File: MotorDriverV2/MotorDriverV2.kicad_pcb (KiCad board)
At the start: 2 copper layers, 20 parts, among them IC1 DRV8871DDARQ1, IC2 DRV8871DDARQ1, IC3 ESP32-S3-WROOM-1U-N4, J1 Power, J2 Out_A, J3 Conn_01x10_Pin, J4 Out_B, U1 USBLC6-2SC6

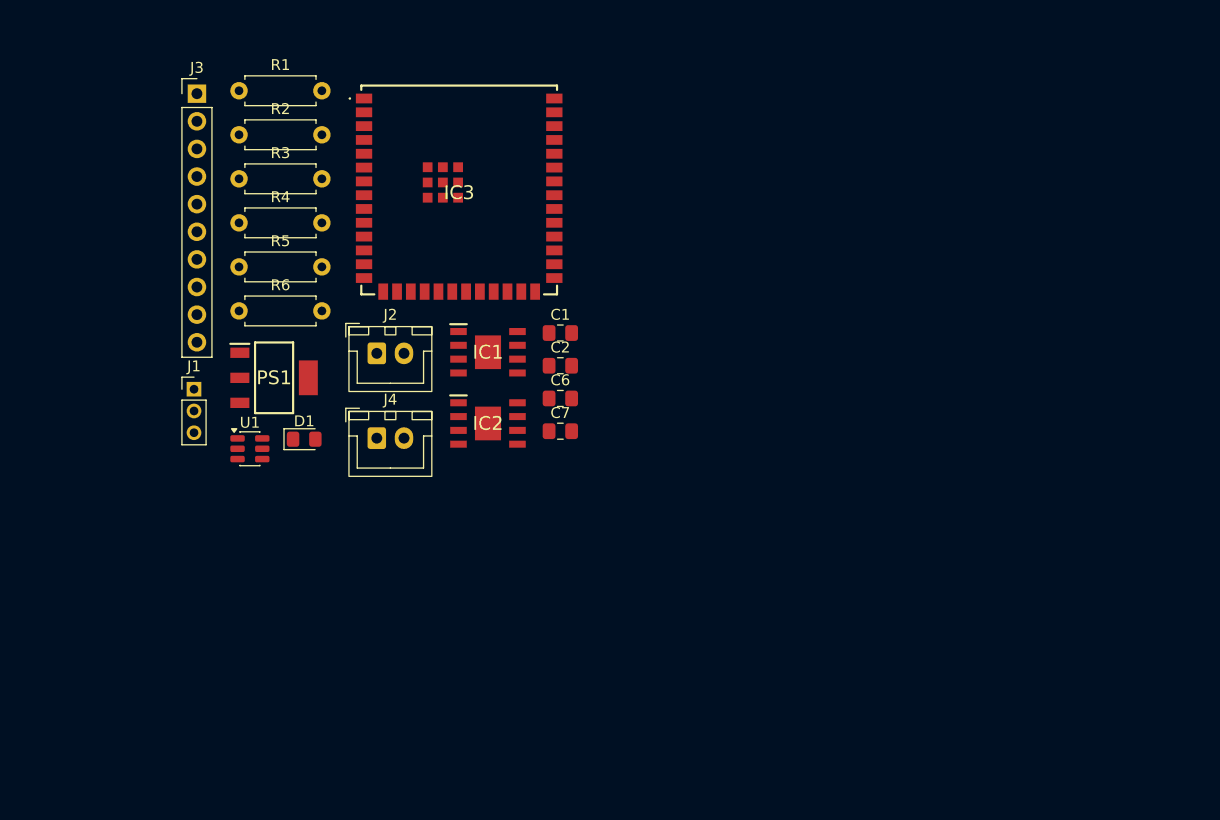
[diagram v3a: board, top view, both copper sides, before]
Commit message: UPDATE: Symbols and footprint added, need to finish layout
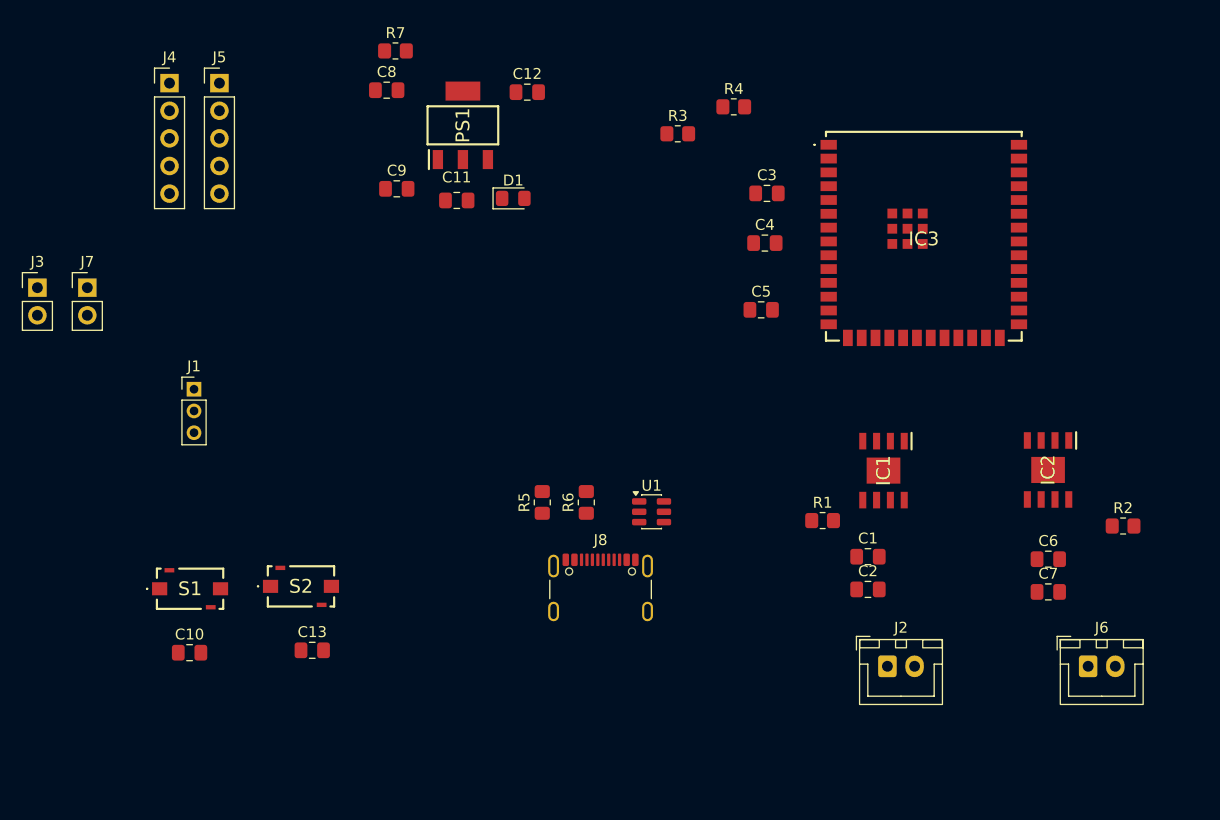
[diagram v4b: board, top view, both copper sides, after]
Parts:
- added C10: 0.1uF, Capacitor_SMD:C_0805_2012Metric_Pad1.18x1.45mm_HandSolder, F.Cu at (79.0, 84.7)
- added C11: 0.1uF, Capacitor_SMD:C_0805_2012Metric_Pad1.18x1.45mm_HandSolder, F.Cu at (103.5, 43.1)
- added C12: 10uF, Capacitor_SMD:C_0805_2012Metric_Pad1.18x1.45mm_HandSolder, F.Cu at (110.0, 33.1)
- added C13: 0.1uF, Capacitor_SMD:C_0805_2012Metric_Pad1.18x1.45mm_HandSolder, F.Cu at (90.2, 84.5)
- added C3: 10uF, Capacitor_SMD:C_0805_2012Metric_Pad1.18x1.45mm_HandSolder, F.Cu at (132.1, 42.5)
- added C4: 0.1uF, Capacitor_SMD:C_0805_2012Metric_Pad1.18x1.45mm_HandSolder, F.Cu at (131.9, 47.0)
- added C5: 1uF, Capacitor_SMD:C_0805_2012Metric_Pad1.18x1.45mm_HandSolder, F.Cu at (131.5, 53.2)
- added C8: 10uF, Capacitor_SMD:C_0805_2012Metric_Pad1.18x1.45mm_HandSolder, F.Cu at (97.1, 33.0)
- added C9: 0.1uF, Capacitor_SMD:C_0805_2012Metric_Pad1.18x1.45mm_HandSolder, F.Cu at (98.0, 42.0)
- added J4: Conn_01x05_Pin, Connector_PinHeader_2.54mm:PinHeader_1x05_P2.54mm_Vertical, F.Cu at (77.1, 32.3)
- added J5: Conn_01x05_Pin, Connector_PinHeader_2.54mm:PinHeader_1x05_P2.54mm_Vertical, F.Cu at (81.7, 32.3)
- added J7: Conn_01x02_Pin, Connector_PinHeader_2.54mm:PinHeader_1x02_P2.54mm_Vertical, F.Cu at (69.5, 51.1)
- added J8: USB_C_Receptacle_USB2.0_16P, Connector_USB:USB_C_Receptacle_GCT_USB4105-xx-A_16P_TopMnt_Horizontal, F.Cu at (116.8, 79.8)
- added R3: zero, Resistor_SMD:R_0805_2012Metric_Pad1.20x1.40mm_HandSolder, F.Cu at (123.8, 37.0)
- added S1: PTS636SKG25JSMTR_LFS, PTS636SKG25JSMTR_LFS:PTS636SKG25JSMTRLFS, F.Cu at (79.0, 78.8)
- added S2: PTS636SKG25JSMTR_LFS, PTS636SKG25JSMTR_LFS:PTS636SKG25JSMTRLFS, F.Cu at (89.2, 78.6)
- J3: value Conn_01x10_Pin -> Conn_01x02_Pin; footprint Connector_PinHeader_2.54mm:PinHeader_1x10_P2.54mm_Vertical -> Connector_PinHeader_2.54mm:PinHeader_1x02_P2.54mm_Vertical
- R1, R2: footprint Resistor_THT:R_Axial_DIN0207_L6.3mm_D2.5mm_P7.62mm_Horizontal -> Resistor_SMD:R_0805_2012Metric_Pad1.20x1.40mm_HandSolder
- R4: renamed from R3; footprint Resistor_THT:R_Axial_DIN0207_L6.3mm_D2.5mm_P7.62mm_Horizontal -> Resistor_SMD:R_0805_2012Metric_Pad1.20x1.40mm_HandSolder
- R5: renamed from R4; footprint Resistor_THT:R_Axial_DIN0207_L6.3mm_D2.5mm_P7.62mm_Horizontal -> Resistor_SMD:R_0805_2012Metric_Pad1.20x1.40mm_HandSolder
- R6: renamed from R5; footprint Resistor_THT:R_Axial_DIN0207_L6.3mm_D2.5mm_P7.62mm_Horizontal -> Resistor_SMD:R_0805_2012Metric_Pad1.20x1.40mm_HandSolder
- R7: renamed from R6; footprint Resistor_THT:R_Axial_DIN0207_L6.3mm_D2.5mm_P7.62mm_Horizontal -> Resistor_SMD:R_0805_2012Metric_Pad1.20x1.40mm_HandSolder
- moved R2 88.9 mm to (164.8, 73.0)
- moved J6 68.7 mm to (161.6, 85.9)
- moved R1 66.7 mm to (137.2, 72.5)
- moved J2 55.1 mm to (143.1, 85.9)
- moved IC2 51.7 mm to (157.9, 67.9), turned to -90 degrees
- moved C6 47.2 mm to (157.9, 76.1)
- moved C7 47.2 mm to (157.9, 79.1)
- moved R4 46.0 mm to (129.0, 34.5)
- moved IC3 42.9 mm to (146.5, 46.6)
- moved R6 38.6 mm to (115.4, 70.9), turned to 90 degrees
- moved IC1 38.0 mm to (142.8, 67.9), turned to -90 degrees
- moved R5 37.9 mm to (111.4, 70.9), turned to 90 degrees
- moved U1 37.4 mm to (121.4, 71.7)
- moved C2 35.0 mm to (141.3, 78.9)
- moved C1 35.0 mm to (141.3, 75.9)
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- renumbered J4 to J6
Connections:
- IC3 pad 10: unconnected-(IC3-IO17-Pad10) -> /IO_17
- IC3 pad 11: unconnected-(IC3-IO18-Pad11) -> /IO_18
- IC3 pad 13: /IO_19 -> D-
- IC3 pad 14: /IO_20 -> D+
- IC3 pad 15: /IO_03 -> unconnected-(IC3-IO3-Pad15)
- IC3 pad 16: /IO_46 -> unconnected-(IC3-IO46-Pad16)
- IC3 pad 17: /IO_09 -> unconnected-(IC3-IO9-Pad17)
- IC3 pad 18: /IO_10 -> In1_1
- IC3 pad 19: /IO_11 -> In1_2
- IC3 pad 2: +3V3 -> /ESP_3v3
- IC3 pad 21: unconnected-(IC3-IO13-Pad21) -> /IO_13
- IC3 pad 24: unconnected-(IC3-IO47-Pad24) -> In2_1
- IC3 pad 25: unconnected-(IC3-IO48-Pad25) -> In2_2
- IC3 pad 4: In2_1 -> /IO_04
- IC3 pad 5: In2_2 -> /IO_05
- IC3 pad 6: In1_2 -> /IO_06
- IC3 pad 7: In1_1 -> /IO_07
- IC3 pad 8: unconnected-(IC3-IO15-Pad8) -> /IO_15
- IC3 pad 9: unconnected-(IC3-IO16-Pad9) -> /IO_16
- J3 pad 1: GND -> /ESP_3v3
- J3 pad 2: +3V3 -> GND
- R4 pad 1: +3V3 -> /ESP_3v3

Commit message: Final Update
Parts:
- IC1, IC2: value DRV8871DDARQ1 -> DRV8871
- J8: value USB_C_Receptacle_USB2.0_16P -> USB_C
- PS1: value LM1117IMPX-3.3_NOPB -> LM1117-3.3
- moved J3 104.0 mm to (168.7, 59.3)
- moved S1 91.0 mm to (162.0, 41.6), turned to 90 degrees
- moved J5 87.6 mm to (168.7, 42.7)
- moved S2 77.6 mm to (162.0, 51.8), turned to -90 degrees
- moved C13 76.1 mm to (161.5, 57.6)
- moved C10 67.3 mm to (132.2, 43.5), turned to 90 degrees
- moved J1 50.6 mm to (125.0, 82.4), turned to 90 degrees
- moved J7 44.1 mm to (112.9, 59.4)
- moved J4 37.3 mm to (112.9, 42.6)
- moved R7 36.4 mm to (124.6, 54.1)
- moved R6 36.3 mm to (151.5, 74.2), turned to 0 degrees
- moved C8 32.4 mm to (127.2, 45.0)
- moved J2 31.4 mm to (114.3, 73.4), turned to -90 degrees
- moved R5 30.8 mm to (142.1, 74.2), turned to 180 degrees
- moved J8 30.0 mm to (146.7, 81.2)
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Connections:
- J5 pad 1: /IO_13 -> /IO_15
- J5 pad 2: /IO_15 -> /IO_16
- J5 pad 3: /IO_16 -> /IO_17
- J5 pad 4: /IO_17 -> /IO_18
- J5 pad 5: /IO_18 -> /IO_13
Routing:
- net /ESP_3v3: track 0.00 -> 106.4 mm, vias 0 -> 4
- net +5V: track 0.00 -> 82.5 mm, vias 0 -> 5
- net /EN: track 0.00 -> 40.6 mm, vias 0 -> 2
- net +7.4V: track 0.00 -> 40.5 mm, vias 0 -> 4
- net +3V3: track 0.00 -> 40.4 mm
- net /IO_15: track 0.00 -> 36.6 mm, vias 0 -> 1
- net /IO_16: track 0.00 -> 36.1 mm, vias 0 -> 1
- net Out1_2: track 0.00 -> 35.8 mm
- net /IO_17: track 0.00 -> 35.6 mm, vias 0 -> 1
- net /IO_18: track 0.00 -> 35.2 mm, vias 0 -> 1
- net D+: track 0.00 -> 31.9 mm, vias 0 -> 2
- net Out1_1: track 0.00 -> 30.1 mm
- net D-: track 0.00 -> 30.0 mm, vias 0 -> 2
- net /IO_07: track 0.00 -> 26.8 mm, vias 0 -> 1
- net /IO_06: track 0.00 -> 26.2 mm, vias 0 -> 1
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- added copper zone on B.Cu, net GND
- added copper zone on F.Cu, net GND
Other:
- board outline added: 61.9 x 50.3 mm
- board text added: "Advisor: Dr N. Wongkasem"
- board text added: "Lauro Cantu Daniel Drane Jesus Martinez Luis Trevino"
- board text added: "TEAM 4 Senior Design II Spring 2026"

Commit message: Completed PCB's
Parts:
- added G1: LOGO, FFLogo:FFLogo, F.Cu at (120.1, 66.9)
- added G1: LOGO, FFLogo:FFLogo, B.Cu at (122.6, 59.4)

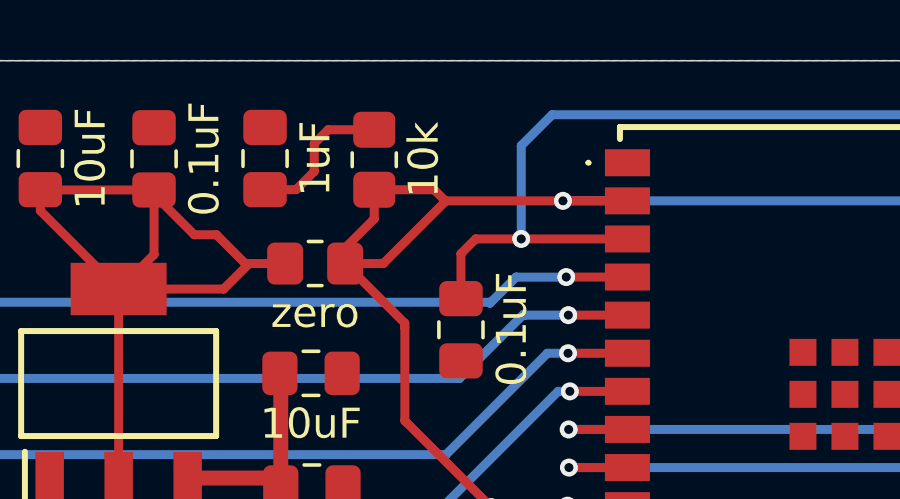
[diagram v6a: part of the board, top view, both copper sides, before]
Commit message: UPDATE: Fix EN pin in ESP motor driver
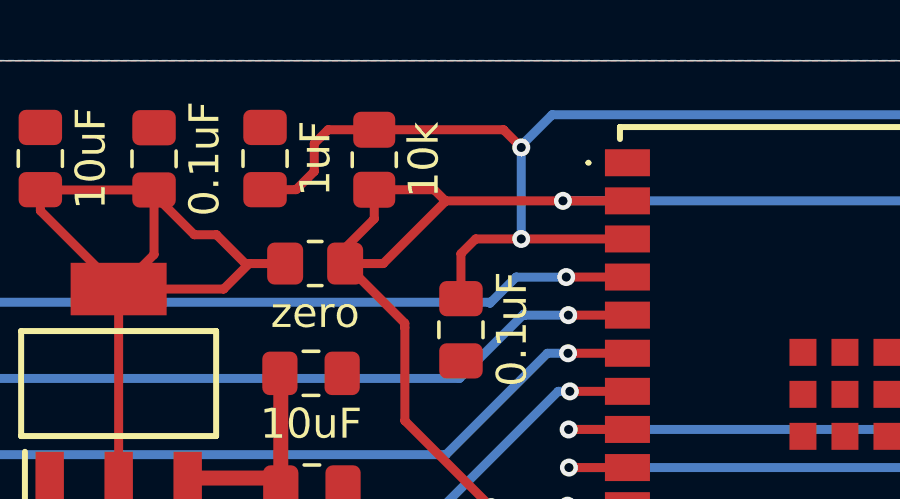
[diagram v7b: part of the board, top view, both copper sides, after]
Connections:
- C5 pad 1: Net-(C5-Pad1) -> /EN
- R4 pad 2: Net-(C5-Pad1) -> /EN
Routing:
- net /EN: track 40.6 -> 50.7 mm, vias 2 -> 3
- net Net-(C5-Pad1): track 5.01 -> 0.00 mm
